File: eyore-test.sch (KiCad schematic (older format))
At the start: 26 parts, among them P1 USB_5PIN_SHELL, P2 CONN_01X04, P3 CONN_01X02, SW1 SW_PUSHBUTTON, SW2 SW_PUSHBUTTON, U1 LD1117S33CTR, U2 STM32F042K, U3 ESP-12E, U4 ESP-12E

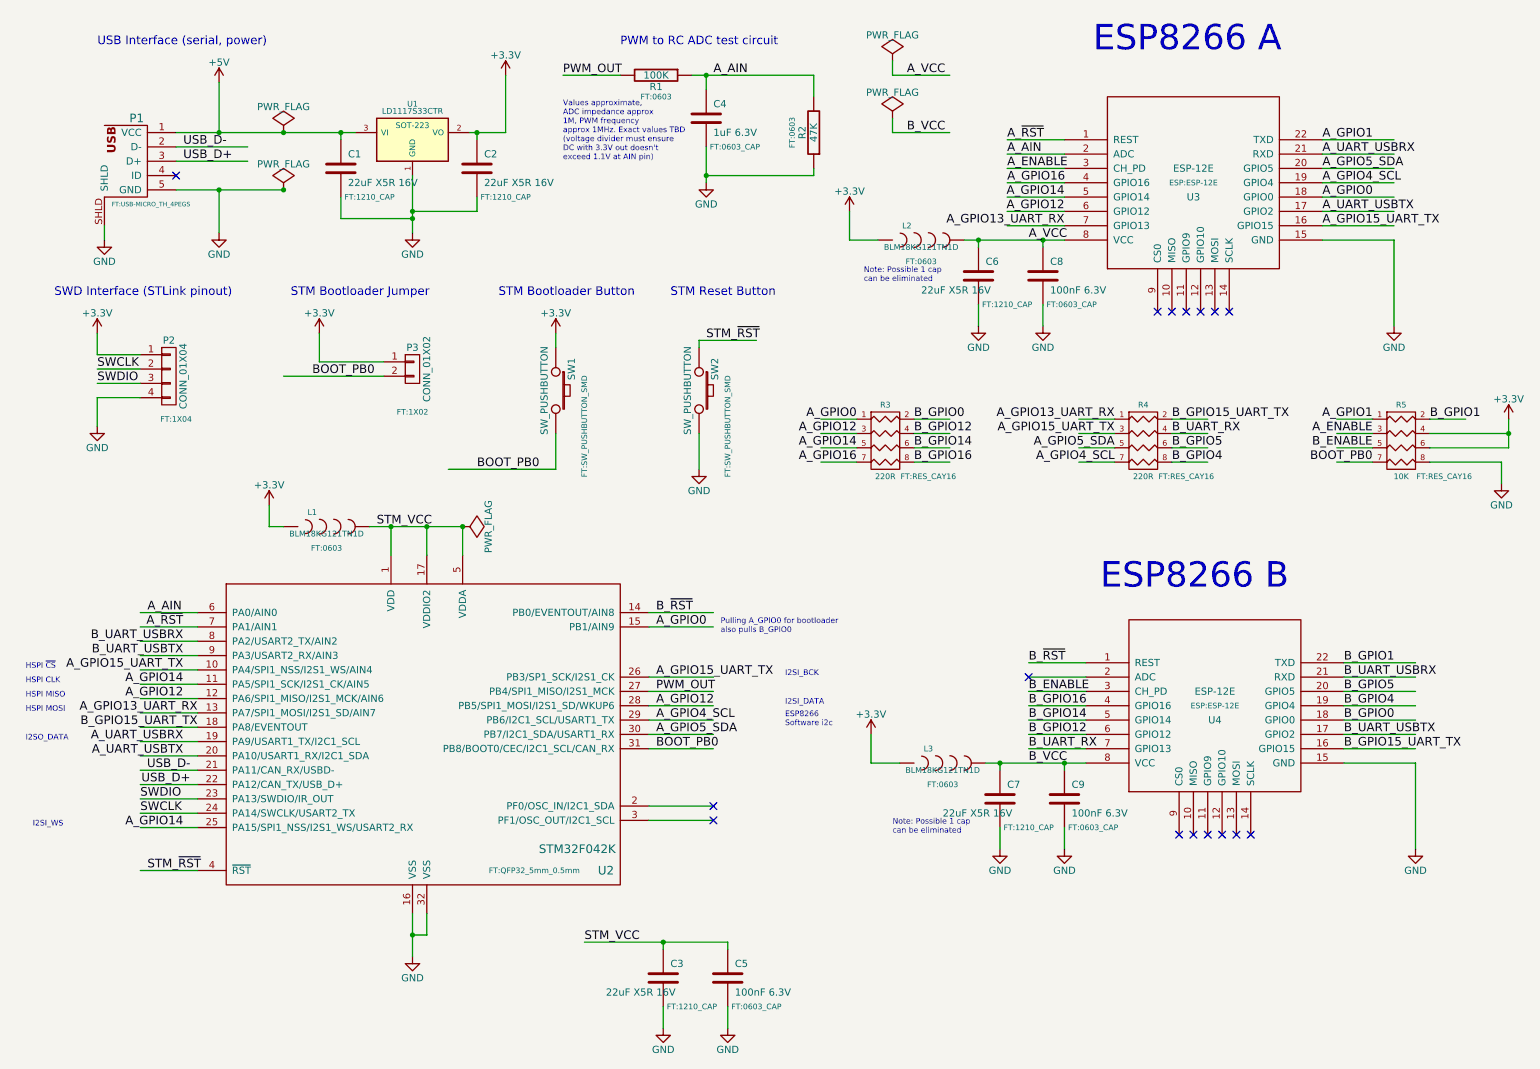
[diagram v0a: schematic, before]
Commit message: Swap STM32F042K for larger STM32F042C, allow routing of ESP SPI port to second STM SPI
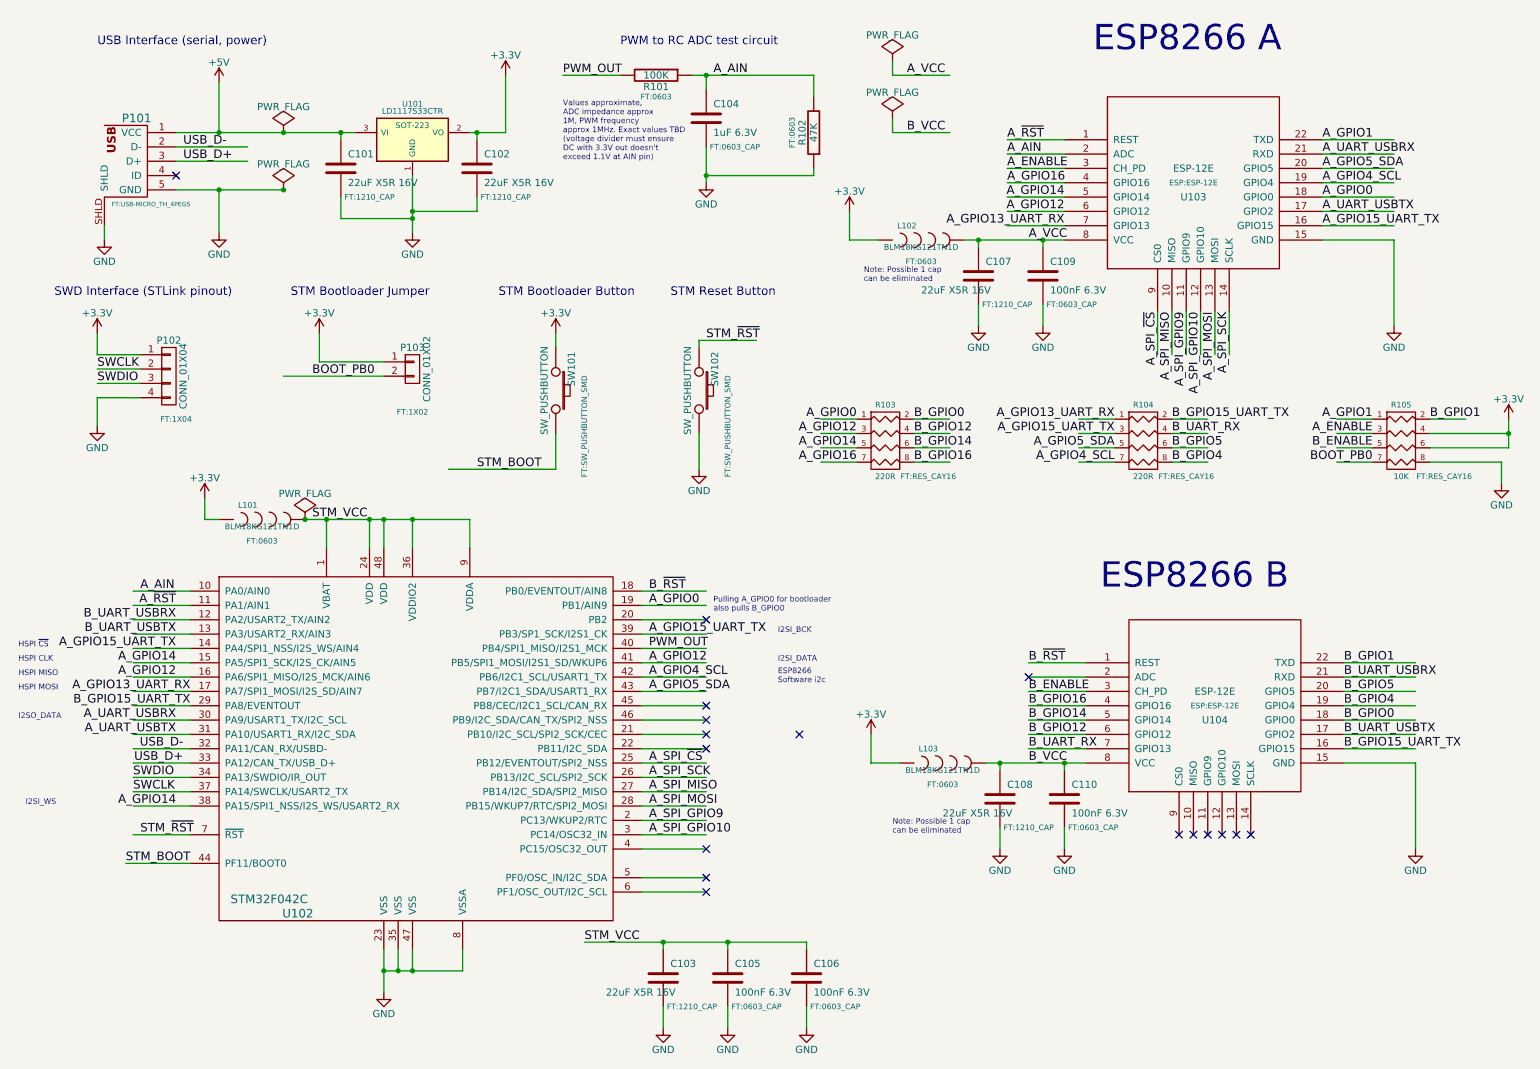
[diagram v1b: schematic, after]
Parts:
- removed U2: STM32F042K, FT:QFP32_5mm_0.5mm, symbol STM32F042K
- added C106: 100nF 6.3V, FT:0603_CAP, symbol CAP
- added U102: STM32F042C, symbol STM32F042C
- renumbered C1 to C101, C2 to C102, C3 to C103, C4 to C104, C5 to C105, C6 to C107, C7 to C108, C8 to C109, C9 to C110, L1 to L101, L2 to L102, L3 to L103, P1 to P101, P2 to P102, P3 to P103, R1 to R101, R2 to R102, R3 to R103, R4 to R104, R5 to R105, SW1 to SW101, SW2 to SW102, U1 to U101, U3 to U103, U4 to U104
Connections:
- net labels added: A_SPI_GPIO10, A_SPI_GPIO9, A_SPI_MISO, A_SPI_MOSI, A_SPI_SCK, A_SPI_~CS, STM_BOOT
- wire segments 155 -> 179
- no-connect marks 16 -> 17
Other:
- moved on the sheet: L101

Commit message: Simplify UART wiring, general cleanup
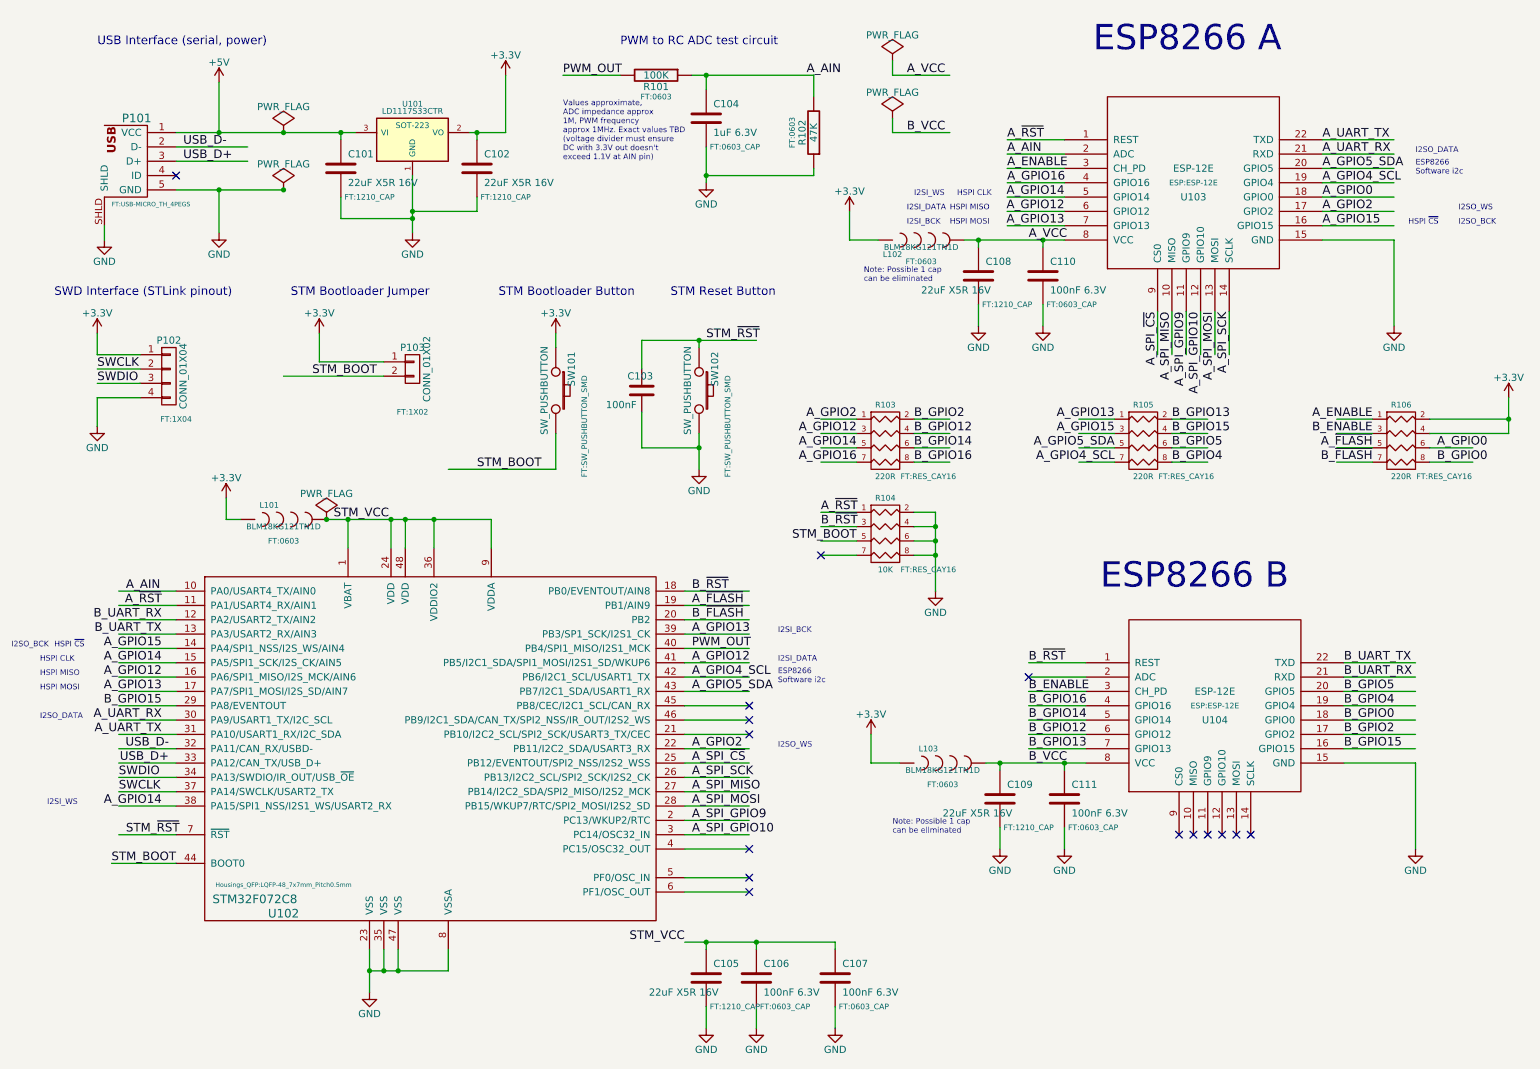
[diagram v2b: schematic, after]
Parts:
- removed U102: STM32F042C, symbol STM32F042C
- added C103: 100nF, symbol C
- added R104: 10K, FT:RES_CAY16, symbol R_PACK4
- added U102: STM32F072C8, Housings_QFP:LQFP-48_7x7mm_Pitch0.5mm, symbol STM32F072C8
- R106: renamed from R105; value 10K -> 220R
- renumbered C103 to C105, C105 to C106, C106 to C107, C107 to C108, C108 to C109, C109 to C110, C110 to C111, R104 to R105
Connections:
- net labels added: A_GPIO13, A_GPIO15, A_GPIO2, A_UART_RX, A_UART_TX, A_~FLASH, B_GPIO13, B_GPIO15, B_GPIO2, B_UART_TX, B_~FLASH
- net labels removed: A_GPIO1, A_GPIO13_UART_RX, A_GPIO15_UART_TX, A_UART_USBRX, A_UART_USBTX, BOOT_PB0, B_GPIO1, B_GPIO15_UART_TX, B_UART_USBRX, B_UART_USBTX
- wire segments 179 -> 190
- no-connect marks 17 -> 15
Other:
- note added: "I2SI_BCK"
- note added: "I2SO_BCK\n"
- note added: "I2SO_WS\n"
- note removed: "Pulling A_GPIO0 for bootloader\nalso pulls B_GPIO0"
- moved on the sheet: C105, C106, C107, L101
